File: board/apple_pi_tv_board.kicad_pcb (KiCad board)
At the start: 4 copper layers, 61 x 85.1 mm, 59 parts, among them J1 RJ45, J2 Micro_SD_Card_Det, J3 5-1775444-8, J4 JTAG_TC2030, J5 BM02B-ACHSS-GAN-TF, U1 HDMI/USB, U10 W25Q128JVS, U11 TPD4EUSB30, U12 RT9742GGJ5, U2 apple tv tos link, U3 RPi_4, U5 RT9742GGJ5, U6 TPD4EUSB30, U7 IRM-V838M3-C/TR1, U8 RP2040, U9 TPS61230DRC, Y1 12MHz

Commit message: started working on rev 2
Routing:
- net /HDMI0_D2_N: track 23.7 -> 21.7 mm
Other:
- outline, holes or cut-outs redrawn

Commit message: got v2 done
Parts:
- U2: moved to F.Cu
- moved C24 68.1 mm to (99.4, 146.7), turned to -90 degrees
- moved C25 66.4 mm to (106.0, 146.3), turned to 0 degrees
- moved C6 6.31 mm to (104.6, 80.6)
- moved C7 6.31 mm to (105.7, 80.6)
- moved U12 4.58 mm to (137.2, 82.0), turned to -90 degrees
- moved R6 3.21 mm to (137.6, 84.6), turned to 180 degrees
- moved J1 2.08 mm to (92.9, 74.7)
- moved U11 2.02 mm to (94.4, 84.5)
- moved U6 2.02 mm to (91.1, 84.5)
- moved U2 0.49 mm to (108.6, 72.1), turned to 0 degrees
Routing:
- net /HDMI_RJ45_USB/HDMI_5v: track 28.1 -> 54.7 mm
- net +5V: track 119.6 -> 113.7 mm
- net /Pico_TOSLINK_IR/toslink: track 115.4 -> 110.3 mm
- net /USB_ID: track 68.4 -> 71.5 mm
- net /TRD0_P: track 76.3 -> 73.4 mm
- net /HDMI0_D2_N: track 21.7 -> 24.1 mm
- net /USB_D-: track 60.5 -> 58.4 mm
- net /TRD2_N: track 89.9 -> 87.9 mm
- net /TRD2_P: track 92.7 -> 90.7 mm
- net /TRD1_N: track 84.1 -> 82.1 mm
- net /TRD3_P: track 85.4 -> 83.4 mm
- net /TRD1_P: track 81.9 -> 79.9 mm
- net /TRD0_N: track 81.1 -> 79.1 mm
- net /TRD3_N: track 86.3 -> 84.3 mm
- net /HDMI_PWR_ON: track 79.4 -> 80.9 mm
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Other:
- outline, holes or cut-outs redrawn

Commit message: worked on new version with rp2350
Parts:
- removed C13, C2: 22u, Capacitor_SMD:C_0402_1005Metric
- removed C18: 100n, Capacitor_SMD:C_0402_1005Metric
- removed R10: 100k, Resistor_SMD:R_0603_1608Metric
- removed R9: 402k, Resistor_SMD:R_0603_1608Metric
- removed U10: W25Q128JVS, Package_SO:SOIC-8_5.23x5.23mm_P1.27mm
- removed U8: RP2040, Package_DFN_QFN:QFN-56-1EP_7x7mm_P0.4mm_EP3.2x3.2mm
- added C10: 4.7u, Capacitor_SMD:C_0402_1005Metric, F.Cu at (104.0, 144.9)
- added C11: 4.7u, Capacitor_SMD:C_0402_1005Metric, F.Cu at (105.0, 144.9)
- added C14: 10u, Capacitor_SMD:C_0402_1005Metric, F.Cu at (120.2, 143.3)
- added L2: 3.3u, Inductor_SMD:L_Murata_DFE201610P, F.Cu at (106.6, 144.7)
- added R12: 33, Resistor_SMD:R_0402_1005Metric, F.Cu at (106.7, 147.7)
- added R13: 10K, Resistor_SMD:R_0402_1005Metric, F.Cu at (104.3, 139.5)
- added U4: RP2350A-QFN60, Package_DFN_QFN:QFN-60-1EP_7x7mm_P0.4mm_EP3.4x3.4mm, F.Cu at (99.4, 142.8)
- C1: value 22u -> 10u
- C12: value 10n -> 8.2n
- C19: value 1u -> 4.7u
- C21: value 10u -> 100n
- C22: value 1u -> 100n
- C29, C30: value 22pF -> 15pF
- C3: value 22u -> 4.7u
- C8: value 100n -> 4.7u; moved to F.Cu
- C9: value 18p -> 10u
- L1: value 1uH -> 18.1uH
- R11: value 1M -> 100K
- U9: value TPS61230DRC -> TPS61232DRC
- Y1: value 12MHz -> ABM8-272-T3
- moved C19 13.5 mm to (93.1, 144.3), turned to 180 degrees
- moved C23 13.3 mm to (106.4, 140.7), turned to 0 degrees
- moved C25 12.9 mm to (93.1, 146.6), turned to 180 degrees
- moved C28 11.4 mm to (94.8, 139.0), turned to 90 degrees
- moved C26 11.1 mm to (97.7, 137.9), turned to 180 degrees
- moved C22 10.3 mm to (106.4, 141.8), turned to 0 degrees
- moved C17 8.74 mm to (99.8, 137.5), turned to 90 degrees
- moved C27 7.37 mm to (102.1, 148.5), turned to -90 degrees
- moved C20 7.18 mm to (100.2, 148.5), turned to -90 degrees
- moved C9 4.69 mm to (119.2, 143.3), turned to 90 degrees
- moved C8 3.93 mm to (104.4, 147.6), turned to 180 degrees
- moved R4 3.60 mm to (90.2, 146.3)
- moved C30 2.25 mm to (90.2, 143.2)
- moved Y1 2.20 mm to (91.5, 140.8)
- moved R5 2.13 mm to (93.1, 143.1)
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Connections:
- C1 pad 1: /Power/power in -> Net-(U9-EN)
- C20 pad 1: +3V3 -> +1V1
- C8 pad 1: +3V3 -> Net-(U4-VREG_AVDD)
- C9 pad 1: +5V -> Net-(U9-EN)
- C9 pad 2: Net-(U9-FB) -> GND
- J3 pad 1: /Power/power in -> Net-(U9-EN)
- J3 pad 2: /Power/power in -> Net-(U9-EN)
- J3 pad 3: /Power/power in -> Net-(U9-EN)
- J3 pad 4: /Power/power in -> Net-(U9-EN)
- L1 pad 1: /Power/power in -> Net-(U9-EN)
- U9 pad 10: /Power/power in -> Net-(U9-EN)
- U9 pad 7: Net-(U9-FB) -> +5V
- U9 pad 9: /Power/power in -> Net-(U9-EN)
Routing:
- net Net-(U9-EN): track 0.00 -> 41.6 mm, vias 0 -> 4
- net /Power/power in: track 39.4 -> 0.00 mm, vias 4 -> 0
- net /Pico_TOSLINK_IR/toslink: track 110.3 -> 89.3 mm
- net Net-(U4-VREG_LX): track 0.00 -> 10.9 mm, vias 0 -> 2
- net Net-(U4-GPIO19): track 36.3 -> 25.5 mm, vias 4 -> 2
- net /swclk: track 83.0 -> 93.6 mm
- net /Pico_TOSLINK_IR/SD0: track 9.63 -> 0.00 mm, vias 1 -> 0
- net /Pico_TOSLINK_IR/SD2: track 9.00 -> 0.00 mm, vias 1 -> 0
- net /Pico_TOSLINK_IR/QSPI_CLK: track 8.23 -> 0.00 mm, vias 1 -> 0
- net /Pico_TOSLINK_IR/SD3: track 7.38 -> 0.00 mm, vias 1 -> 0
- net /Pico_TOSLINK_IR/SD1: track 7.29 -> 0.00 mm, vias 1 -> 0
- net +3V3: track 192.2 -> 185.3 mm, vias 17 -> 19
- net /Pico_TOSLINK_IR/CS: track 6.50 -> 0.00 mm, vias 1 -> 0
- net Net-(U9-FB): track 4.94 -> 0.00 mm
- net Net-(U4-VREG_AVDD): track 0.00 -> 4.78 mm
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- added copper zone on In2.Cu, net Net-(U9-EN)
- removed copper zone on In2.Cu, net /Power/power in

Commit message: updated most stuff, but i completely redid the diff pairs
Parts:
- added D2: LED_Small, LED_SMD:LED_0805_2012Metric, F.Cu at (137.4, 118.8)
- added D3: LED_Small, LED_SMD:LED_0805_2012Metric, F.Cu at (137.4, 109.4)
- added JP1-WL1: SolderJumper_2_Open, Jumper:SolderJumper-2_P1.3mm_Open_TrianglePad1.0x1.5mm, F.Cu at (116.2, 120.5)
- added JP2-BT1: SolderJumper_2_Open, Jumper:SolderJumper-2_P1.3mm_Open_TrianglePad1.0x1.5mm, F.Cu at (120.8, 120.5)
- added JP3-EEPROM1: SolderJumper_2_Open, Jumper:SolderJumper-2_P1.3mm_Open_TrianglePad1.0x1.5mm, F.Cu at (111.2, 120.5)
- added R9: R, Resistor_SMD:R_0402_1005Metric, F.Cu at (137.3, 114.9)
- added TP1: RUN_PG, TestPoint:TestPoint_Pad_D1.5mm, F.Cu at (137.4, 124.0)
- added TP2: Extrst, TestPoint:TestPoint_Pad_D1.5mm, F.Cu at (137.5, 127.5)
- moved J4 39.2 mm to (135.5, 143.2)
- moved U11 1.39 mm to (94.4, 85.9)
- moved U6 1.39 mm to (91.1, 85.9)
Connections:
- J4 pad 1: +3V3 -> unconnected-(J4-VCC-Pad1)
- U11 pad 1: /TRD3_P -> /TRD3_N
- U11 pad 2: /TRD3_N -> /TRD3_P
- U11 pad 4: /TRD2_N -> /TRD2_P
- U11 pad 5: /TRD2_P -> /TRD2_N
- U3 pad 100: unconnected-(U3A-~{EXTRST}-Pad100) -> Net-(U3A-~{EXTRST})
- U3 pad 20: unconnected-(U3A-EEPROM_~{WP}-Pad20) -> Net-(JP3-EEPROM1-B)
- U3 pad 21: unconnected-(U3A-PI_~{LED_ACTIVITY}-Pad21) -> Net-(D3-A)
- U3 pad 78: unconnected-(U3A-GPIO_VREF-Pad78) -> +3V3
- U3 pad 89: unconnected-(U3A-WL_~{DISABLE}-Pad89) -> Net-(JP1-WL1-B)
- U3 pad 91: unconnected-(U3A-BT_~{DISABLE}-Pad91) -> Net-(JP2-BT1-B)
- U3 pad 92: unconnected-(U3A-RUN_PG-Pad92) -> Net-(U3A-RUN_PG)
- U3 pad 95: unconnected-(U3A-PI_LED_~{PWR}-Pad95) -> Net-(D2-A)
- U6 pad 1: /TRD1_P -> /TRD1_N
- U6 pad 2: /TRD1_N -> /TRD1_P
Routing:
- net Net-(D3-A): track 0.00 -> 47.1 mm, vias 0 -> 2
- net /TRD1_N: track 82.1 -> 54.1 mm
- net /TRD2_P: track 90.7 -> 63.8 mm
- net /TRD2_N: track 87.9 -> 62.5 mm, vias 2 -> 0
- net Net-(D2-A): track 0.00 -> 24.8 mm, vias 0 -> 2
- net /TRD1_P: track 79.9 -> 56.1 mm, vias 3 -> 2
- net /TRD3_P: track 83.4 -> 59.7 mm, vias 2 -> 0
- net Net-(U3A-RUN_PG): track 0.00 -> 20.6 mm, vias 0 -> 2
- net /TRD3_N: track 84.3 -> 65.1 mm
- net /Pico_TOSLINK_IR/~{RESET}: track 83.0 -> 64.4 mm
- net Net-(U3A-~{EXTRST}): track 0.00 -> 18.4 mm, vias 0 -> 2
- net /TRD0_N: track 79.1 -> 61.4 mm, vias 4 -> 2
- net Net-(JP1-WL1-B): track 0.00 -> 14.7 mm
- net Net-(JP2-BT1-B): track 0.00 -> 13.2 mm
- net Net-(JP3-EEPROM1-B): track 0.00 -> 11.3 mm, vias 0 -> 2
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- added copper zone on In2.Cu, net GND

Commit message: almost v0.3
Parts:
- L1: value 18.1uH -> 1uH; footprint Inductor_SMD:L_Coilcraft_XxL4020 -> MDA4020:MDA4020
- U4: value RP2350A-QFN60 -> RP2354A
- moved R11 0.66 mm to (110.0, 137.7)
- moved L1 0.23 mm to (114.6, 137.3)
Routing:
- net /TRD3_N: track 65.1 -> 59.5 mm
- net /TRD0_N: track 61.4 -> 63.7 mm
- net /TRD1_N: track 54.1 -> 56.1 mm
- net /TRD2_N: track 62.5 -> 63.9 mm
- net Net-(U9-PG): track 5.59 -> 6.62 mm
- net /HDMI0_D2_P: track 21.8 -> 22.8 mm
- net /SD_CMD: track 44.6 -> 43.6 mm
- net GND: track 154.3 -> 153.7 mm
- net /HDMI0_D1_N: track 25.6 -> 25.1 mm
- net /HDMI0_D1_P: track 25.6 -> 25.1 mm
- net /swclk: vias 4 -> 3

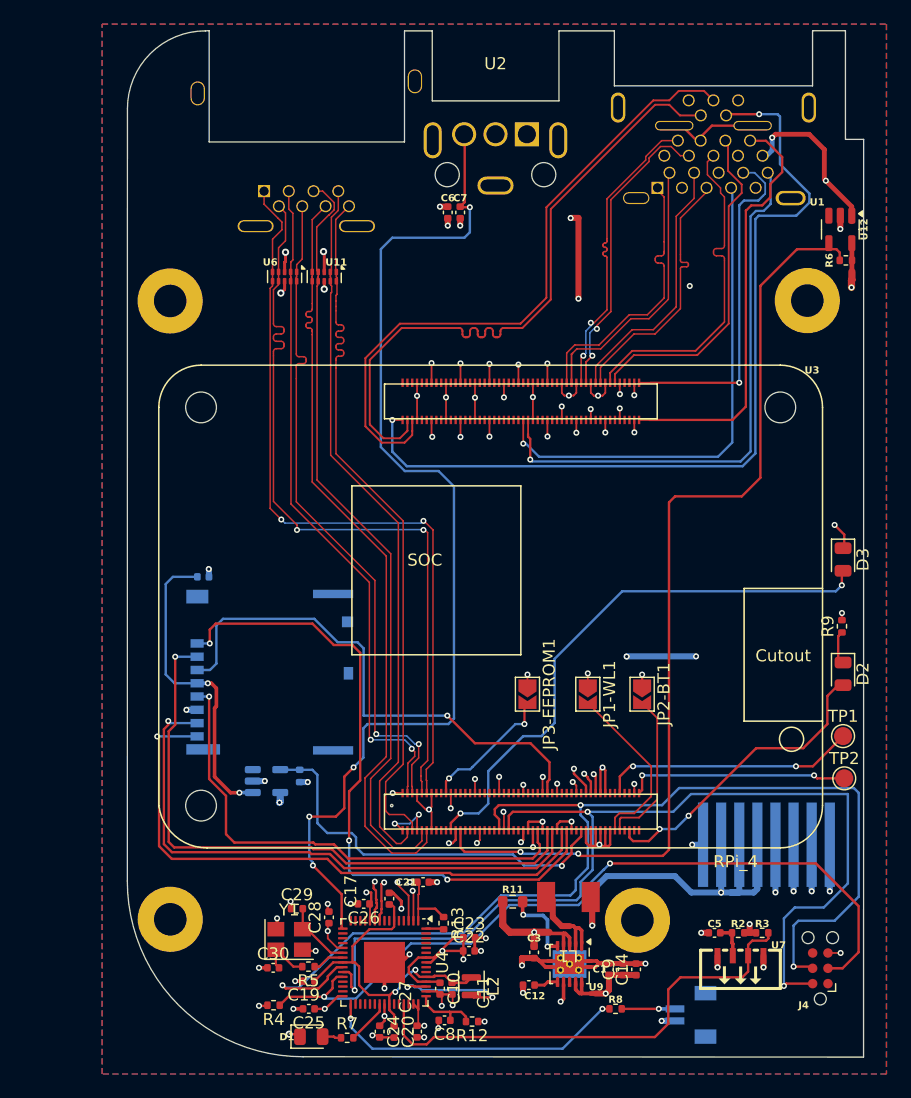
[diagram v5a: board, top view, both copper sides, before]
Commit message: going to add the magnetic transformer which will messs a lot of stuff up
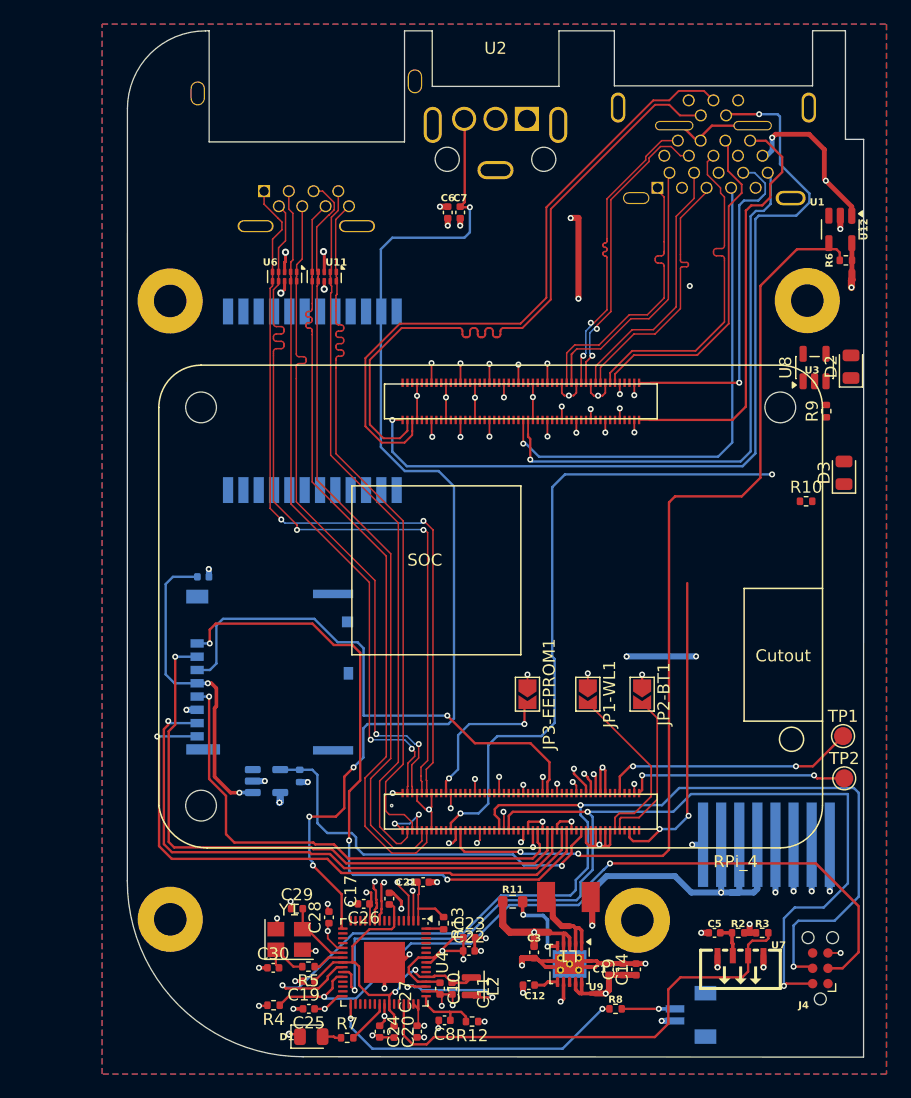
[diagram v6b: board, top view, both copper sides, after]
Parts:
- added R10: R, Resistor_SMD:R_0402_1005Metric, F.Cu at (134.3, 104.5)
- added T1: H5007NL, H5007NL:SOIC127P1600X551-24N, B.Cu at (93.4, 96.2)
- added U8: 74LVC1G07, Package_TO_SOT_SMD:SOT-23-5, F.Cu at (135.0, 93.5)
- moved D2 25.5 mm to (138.1, 93.4), turned to 90 degrees
- moved R9 17.9 mm to (136.0, 97.1)
- moved D3 7.19 mm to (137.5, 102.2), turned to 90 degrees
- moved U2 1.28 mm to (108.6, 70.8)
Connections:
- C1 pad 1: Net-(U9-EN) -> /Power/power in
- C14 pad 1: Net-(U9-EN) -> /Power/power in
- C9 pad 1: Net-(U9-EN) -> /Power/power in
- D2 pad 2: Net-(D2-A) -> +3V3
- D3 pad 1: GND -> Net-(D3-K)
- D3 pad 2: Net-(D3-A) -> +3V3
- J3 pad 1: Net-(U9-EN) -> GND
- J3 pad 2: Net-(U9-EN) -> GND
- J3 pad 3: Net-(U9-EN) -> GND
- J3 pad 4: Net-(U9-EN) -> GND
- J3 pad 6: GND -> /Power/power in
- J3 pad 7: GND -> /Power/power in
- J3 pad 8: GND -> /Power/power in
- L1 pad 1: Net-(U9-EN) -> /Power/power in
- R9 pad 1: Net-(D2-K) -> Net-(R9-Pad1)
- R9 pad 2: GND -> Net-(D2-K)
- U3 pad 21: Net-(D3-A) -> Net-(U3A-PI_~{LED_ACTIVITY})
- U3 pad 95: Net-(D2-A) -> Net-(U3A-PI_LED_~{PWR})
- U9 pad 10: Net-(U9-EN) -> /Power/power in
- U9 pad 9: Net-(U9-EN) -> /Power/power in
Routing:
- net Net-(U3A-PI_~{LED_ACTIVITY}): track 0.00 -> 53.8 mm, vias 0 -> 2
- net Net-(D3-A): track 47.1 -> 0.00 mm, vias 2 -> 0
- net Net-(U9-EN): track 41.5 -> 0.00 mm, vias 4 -> 0
- net Net-(U3A-PI_LED_~{PWR}): track 0.00 -> 25.9 mm, vias 0 -> 2
- net Net-(D2-A): track 24.8 -> 0.00 mm, vias 2 -> 0
- net /Power/power in: track 0.00 -> 19.7 mm, vias 0 -> 4
- net GND: track 153.7 -> 172.6 mm, vias 89 -> 87
- net Net-(D2-K): track 2.62 -> 0.00 mm
- net Net-(JP3-EEPROM1-B): track 11.3 -> 12.9 mm
- added copper zone on In2.Cu, net /Power/power in
- removed copper zone on In2.Cu, net Net-(U9-EN)
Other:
- outline, holes or cut-outs redrawn

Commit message: started more ethernet adding stuff
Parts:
- added C13: C_Small, Capacitor_SMD:C_0402_1005Metric, F.Cu at (71.3, 107.8)
- added C15: C_Small, Capacitor_SMD:C_0402_1005Metric, F.Cu at (71.3, 109.8)
- added C16: C_Small, Capacitor_SMD:C_0402_1005Metric, F.Cu at (71.3, 111.7)
- added C2: C_Small, Capacitor_SMD:C_0402_1005Metric, F.Cu at (71.3, 105.8)
- added R14: 75, Resistor_SMD:R_0402_1005Metric, F.Cu at (72.0, 96.8)
- added R15: 75, Resistor_SMD:R_0402_1005Metric, F.Cu at (72.0, 98.8)
- added R16: 75, Resistor_SMD:R_0402_1005Metric, F.Cu at (72.0, 100.8)
- added R17: 75, Resistor_SMD:R_0402_1005Metric, F.Cu at (72.0, 102.8)
- moved U6 35.1 mm to (99.3, 120.0), turned to 90 degrees
- moved U11 35.0 mm to (102.4, 120.0), turned to 90 degrees
- turned T1 to 90 degrees
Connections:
- J1 pad 1: /TRD0_P -> unconnected-(J1-Pad1)
- J1 pad 2: /TRD0_N -> unconnected-(J1-Pad2)
- J1 pad 3: /TRD1_P -> unconnected-(J1-Pad3)
- J1 pad 4: /TRD1_N -> unconnected-(J1-Pad4)
- J1 pad 5: /TRD2_P -> unconnected-(J1-Pad5)
- J1 pad 6: /TRD2_N -> unconnected-(J1-Pad6)
- J1 pad 7: /TRD3_P -> unconnected-(J1-Pad7)
- J1 pad 8: /TRD3_N -> unconnected-(J1-Pad8)
- T1 pad 1: unconnected-(T1-Pad1) -> Net-(T1-TCT1)
- T1 pad 10: unconnected-(T1-Pad10) -> Net-(T1-TCT4)
- T1 pad 11: unconnected-(T1-Pad11) -> /TRD3_N
- T1 pad 12: unconnected-(T1-Pad12) -> /TRD3_P
- T1 pad 13: unconnected-(T1-Pad13) -> /HDMI_RJ45_USB/MX3_P
- T1 pad 14: unconnected-(T1-Pad14) -> /HDMI_RJ45_USB/MX3_N
- T1 pad 15: unconnected-(T1-Pad15) -> /HDMI_RJ45_USB/MCT3
- T1 pad 16: unconnected-(T1-Pad16) -> /HDMI_RJ45_USB/MX2_P
- T1 pad 17: unconnected-(T1-Pad17) -> /HDMI_RJ45_USB/MX2_N
- T1 pad 18: unconnected-(T1-Pad18) -> /HDMI_RJ45_USB/MCT2
- T1 pad 19: unconnected-(T1-Pad19) -> /HDMI_RJ45_USB/MX1_P
- T1 pad 2: unconnected-(T1-Pad2) -> /TRD0_N
- T1 pad 20: unconnected-(T1-Pad20) -> /HDMI_RJ45_USB/MX1_N
- T1 pad 21: unconnected-(T1-Pad21) -> /HDMI_RJ45_USB/MCT1
- T1 pad 22: unconnected-(T1-Pad22) -> /HDMI_RJ45_USB/MX0_P
- T1 pad 23: unconnected-(T1-Pad23) -> /HDMI_RJ45_USB/MX0_N
- T1 pad 24: unconnected-(T1-Pad24) -> /HDMI_RJ45_USB/MCT0
- T1 pad 3: unconnected-(T1-Pad3) -> /TRD0_P
- T1 pad 4: unconnected-(T1-Pad4) -> Net-(T1-TCT2)
- T1 pad 5: unconnected-(T1-Pad5) -> /TRD1_N
- T1 pad 6: unconnected-(T1-Pad6) -> /TRD1_P
- T1 pad 7: unconnected-(T1-Pad7) -> Net-(T1-TCT3)
- T1 pad 8: unconnected-(T1-Pad8) -> /TRD2_N
- T1 pad 9: unconnected-(T1-Pad9) -> /TRD2_P
- U11 pad 1: /TRD3_N -> /TRD1_P
- U11 pad 2: /TRD3_P -> /TRD1_N
- U11 pad 4: /TRD2_P -> unconnected-(U11-D2+-Pad4)
- U11 pad 5: /TRD2_N -> unconnected-(U11-D2--Pad5)
- U3 pad 11: /TRD2_N -> /TRD2_P
- U3 pad 9: /TRD2_P -> /TRD2_N
- U6 pad 1: /TRD1_N -> /TRD3_N
- U6 pad 2: /TRD1_P -> /TRD3_P
- U6 pad 4: /TRD0_N -> /TRD2_N
- U6 pad 5: /TRD0_P -> /TRD2_P
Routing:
- net /TRD3_P: track 59.7 -> 0.00 mm
- net /TRD3_N: track 59.5 -> 0.00 mm
- net /TRD2_N: track 63.9 -> 7.30 mm
- net /TRD2_P: track 63.8 -> 7.29 mm
- net /TRD1_P: track 56.3 -> 8.48 mm, vias 2 -> 0
- net /TRD1_N: track 56.1 -> 8.48 mm, vias 2 -> 0
- net /TRD0_N: track 63.7 -> 22.3 mm, vias 2 -> 1
- net /TRD0_P: track 63.8 -> 23.4 mm, vias 2 -> 1
- net GND: track 172.6 -> 164.9 mm, vias 87 -> 83

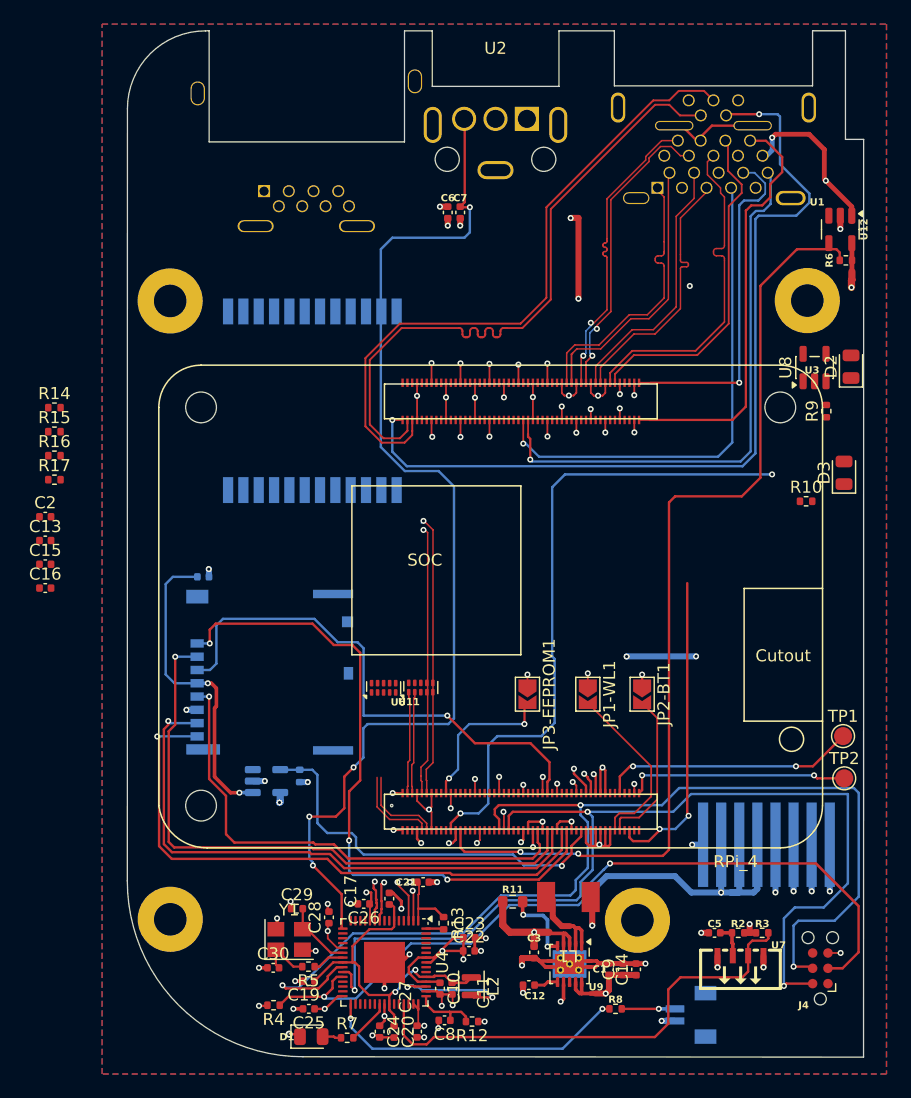
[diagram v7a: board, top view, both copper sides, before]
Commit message: added the real micro sd card slot
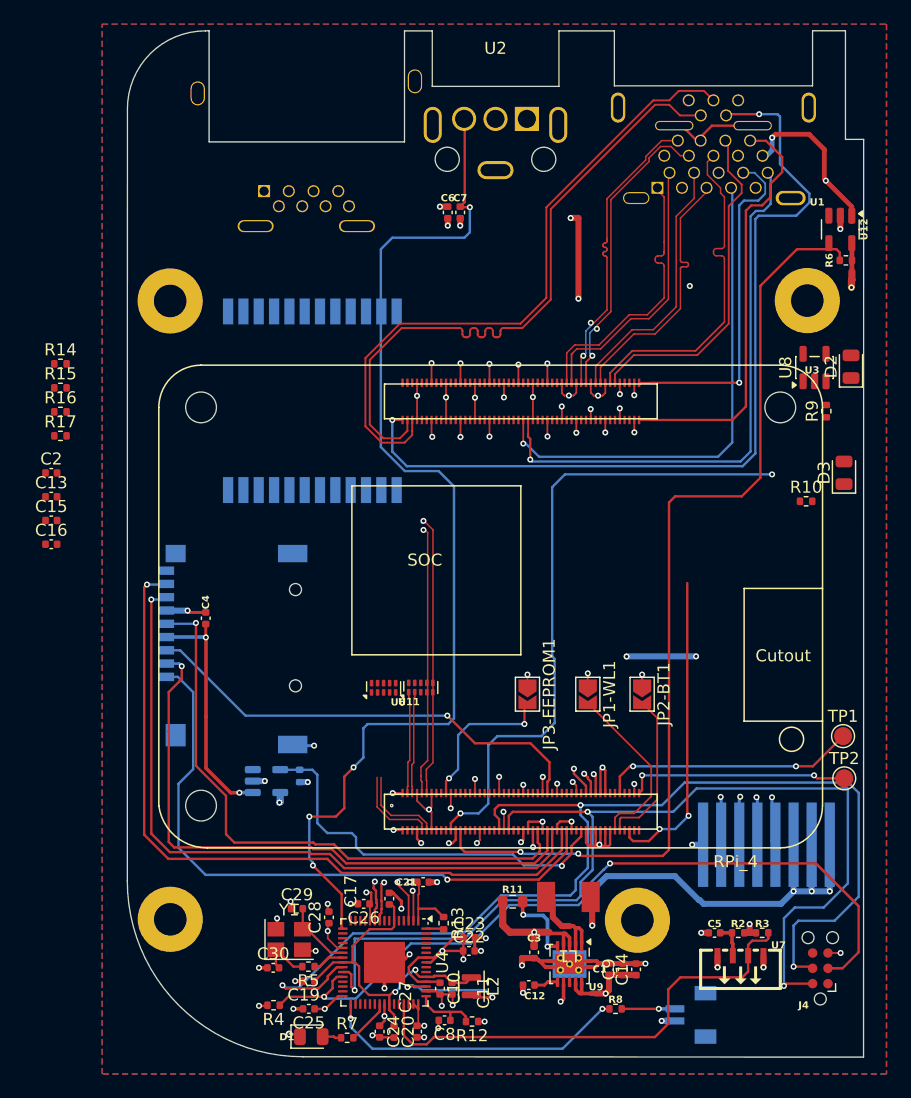
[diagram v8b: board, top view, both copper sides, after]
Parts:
- removed J2: Micro_SD_Card_Det, greencharge-footprints:MICRO_SD_MOLEX_503398-1892
- added MICRO_SD1: TF-01A, MicroSD:TF-01A, B.Cu at (88.5, 116.9)
- C4: moved to F.Cu
- moved C13 3.66 mm to (71.8, 104.2)
- moved C15 3.66 mm to (71.8, 106.1)
- moved C16 3.66 mm to (71.8, 108.1)
- moved R16 3.66 mm to (72.5, 97.1)
- moved C2 3.66 mm to (71.8, 102.2)
- moved R14 3.66 mm to (72.5, 93.2)
- moved R15 3.66 mm to (72.5, 95.1)
- moved R17 3.66 mm to (72.5, 99.1)
- moved C4 3.44 mm to (84.6, 114.2), turned to 90 degrees
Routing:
- net /Power/power in: track 19.7 -> 46.6 mm, vias 4 -> 5
- net GND: track 164.9 -> 147.7 mm, vias 83 -> 84
- net /SD_DAT1: track 49.4 -> 60.9 mm
- net /SD_DAT0: track 48.2 -> 57.5 mm
- net /SD_CLK: track 41.9 -> 49.9 mm
- net /HDMI_RJ45_USB/SD_PWR: track 26.2 -> 20.0 mm
- net /SD_CMD: track 43.6 -> 38.3 mm
- net /SD_DAT2: track 55.4 -> 52.2 mm, vias 3 -> 1
- net /SD_DAT3: track 51.6 -> 50.6 mm
- net /swdio: track 86.2 -> 86.9 mm
